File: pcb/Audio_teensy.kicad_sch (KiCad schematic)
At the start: 20 parts, among them J1 0855025008, J2 SSM-114-L-SV-BE, J3 SSM-114-L-SV-BE, J4 MJ-3523-SMT, J5 MJ-3523-SMT, U1 Teensy 3.2, U2 AP7313, U3 SGTL5000

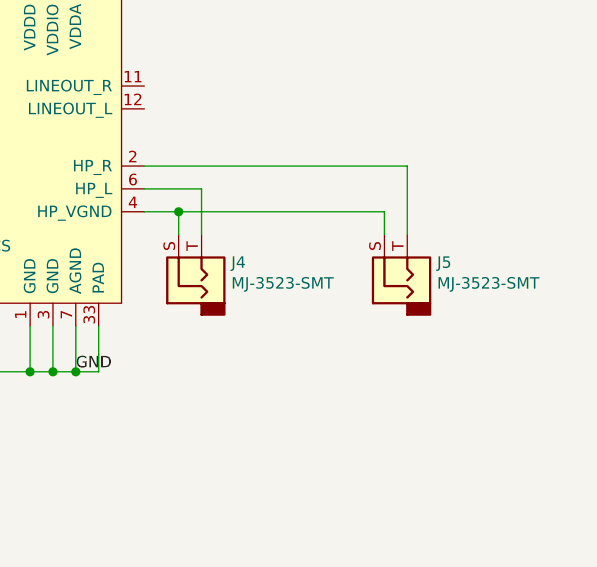
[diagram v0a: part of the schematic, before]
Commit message: changed to through hole components
rearranged mono jacks to point towards opposite sides
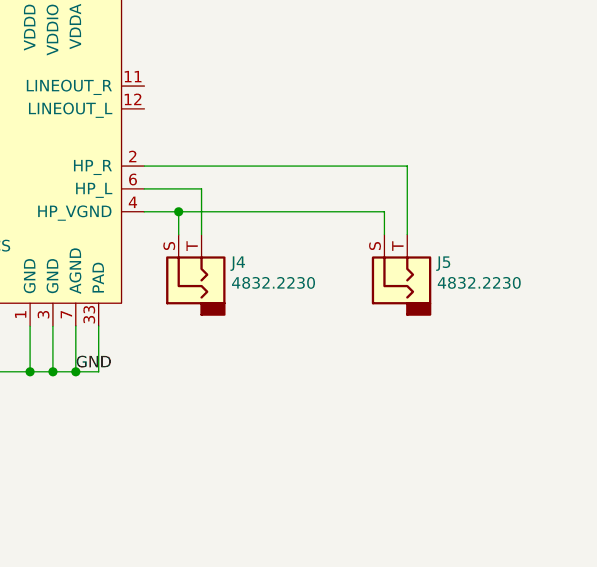
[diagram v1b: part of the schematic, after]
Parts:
- J1: footprint asl_footprints:RJ45_SMD -> asl_footprints:RJ45_THP_Vertical
- J4, J5: value MJ-3523-SMT -> 4832.2230; footprint asl_footprints:MonoJack -> asl_footprints:mono_jack_throughhole
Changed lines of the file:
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@@
   (paper "A4")
   (title_block
-    (date "2019-11-08")
-    (rev "1.1")
+    (date "2021-09-01")
+    (rev "1.2")
   )
   (junction (at 130.81 59.69) (diameter 1.016) (color 0 0 0 0))
@@
       (effects (font (size 1.27 1.27)) (justify right))
     )
-    (property "Value" "MJ-3523-SMT" (id 1) (at 207.772 122.2502 90)
-      (effects (font (size 1.27 1.27)) (justify right))
-    )
-    (property "Footprint" "asl_footprints:MonoJack" (id 2) (at 208.28 121.92 0)
-      (effects (font (size 1.27 1.27)) hide)
-    )
-    (property "Datasheet" "https://www.digikey.com/products/en?keywords=CP-3523MJCT-ND" (id 3) (at 204.47 121.92 0)
+    (property "Value" "4832.2230" (id 1) (at 207.772 122.2502 90)
+      (effects (font (size 1.27 1.27)) (justify right))
+    )
+    (property "Footprint" "asl_footprints:mono_jack_throughhole" (id 2) (at 208.28 121.92 0)
+      (effects (font (size 1.27 1.27)) hide)
+    )
+    (property "Datasheet" "https://www.digikey.com/en/products/detail/4832.2230/486-3417-ND/1731054?itemSeq=375577354" (id 3) (at 204.47 121.92 0)
       (effects (font (size 1.27 1.27)) hide)
     )
@@
       (effects (font (size 1.27 1.27)) (justify right))
     )
-    (property "Value" "MJ-3523-SMT" (id 1) (at 230.632 122.2502 90)
-      (effects (font (size 1.27 1.27)) (justify right))
-    )
-    (property "Footprint" "asl_footprints:MonoJack" (id 2) (at 231.14 121.92 0)
-      (effects (font (size 1.27 1.27)) hide)
-    )
-    (property "Datasheet" "https://www.digikey.com/products/en?keywords=CP-3523MJCT-ND" (id 3) (at 227.33 121.92 0)
+    (property "Value" "4832.2230" (id 1) (at 230.632 122.2502 90)
+      (effects (font (size 1.27 1.27)) (justify right))
+    )
+    (property "Footprint" "asl_footprints:mono_jack_throughhole" (id 2) (at 231.14 121.92 0)
+      (effects (font (size 1.27 1.27)) hide)
+    )
+    (property "Datasheet" "https://www.digikey.com/en/products/detail/4832.2230/486-3417-ND/1731054?itemSeq=375577354" (id 3) (at 227.33 121.92 0)
       (effects (font (size 1.27 1.27)) hide)
     )
@@
       (effects (font (size 1.27 1.27)) (justify left))
     )
-    (property "Footprint" "asl_footprints:RJ45_SMD" (id 2) (at 54.61 74.93 0)
+    (property "Footprint" "asl_footprints:RJ45_THP_Vertical" (id 2) (at 54.61 74.93 0)
       (effects (font (size 1.27 1.27)) hide)
     )
@@
     )
     (path "/00000000-0000-0000-0000-00005dbb4566"
-      (reference "J1") (unit 1) (value "0855025008") (footprint "asl_footprints:RJ45_SMD")
+      (reference "J1") (unit 1) (value "0855025008") (footprint "asl_footprints:RJ45_THP_Vertical")
     )
     (path "/00000000-0000-0000-0000-00005dc200bf"
@@
     )
     (path "/00000000-0000-0000-0000-00005dbb2449"
-      (reference "J4") (unit 1) (value "MJ-3523-SMT") (footprint "asl_footprints:MonoJack")
+      (reference "J4") (unit 1) (value "4832.2230") (footprint "asl_footprints:mono_jack_throughhole")
     )
     (path "/00000000-0000-0000-0000-00005dbb640c"
-      (reference "J5") (unit 1) (value "MJ-3523-SMT") (footprint "asl_footprints:MonoJack")
+      (reference "J5") (unit 1) (value "4832.2230") (footprint "asl_footprints:mono_jack_throughhole")
     )
     (path "/00000000-0000-0000-0000-00005dbd3e4c"

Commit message: pcb v1.3
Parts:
- renumbered C6 to C4, C7 to C5, C5 to C6, C4 to C7, J4 to J2, J5 to J3, J2 to J4, J3 to J5, R3 to R1, R1 to R3, U2 to U1, U1 to U2
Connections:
- no-connect marks 20 -> 22
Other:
- note added: "Left"
- note added: "Right"
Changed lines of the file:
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@@
   (paper "A4")
   (title_block
-    (date "2021-09-01")
-    (rev "1.2")
+    (date "2021-10-12")
+    (rev "1.3")
   )
   (junction (at 130.81 59.69) (diameter 1.016) (color 0 0 0 0))
@@
   (no_connect (at 144.78 105.41))
   (no_connect (at 144.78 107.95))
+  (no_connect (at 198.12 100.33))
+  (no_connect (at 198.12 102.87))
   (wire (pts (xy 64.77 80.01) (xy 93.98 80.01))
     (stroke (width 0) (type solid) (color 0 0 0 0))
@@
     (effects (font (size 1.27 1.27)) (justify left bottom))
   )
+  (text "Left" (at 203.2 129.54 0)
+    (effects (font (size 1.27 1.27)) (justify left bottom))
+  )
+  (text "Right" (at 224.79 129.54 0)
+    (effects (font (size 1.27 1.27)) (justify left bottom))
+  )
   (label "GND" (at 66.04 82.55 0)
     (effects (font (size 1.27 1.27)) (justify left bottom))
@@
   (symbol (lib_id "Device:R_Small_US") (at 86.36 110.49 0) (unit 1)
     (in_bom yes) (on_board yes)
-    (property "Reference" "R1" (id 0) (at 88.0872 109.3216 0)
+    (property "Reference" "R3" (id 0) (at 88.0872 109.3216 0)
       (effects (font (size 1.27 1.27)) (justify left))
     )
@@
   (symbol (lib_id "Device:R_Small_US") (at 158.75 90.17 0) (unit 1)
     (in_bom yes) (on_board yes)
-    (property "Reference" "R3" (id 0) (at 160.4772 89.0016 0)
+    (property "Reference" "R1" (id 0) (at 160.4772 89.0016 0)
       (effects (font (size 1.27 1.27)) (justify left))
     )
@@
   (symbol (lib_id "Device:C") (at 153.67 124.46 0) (unit 1)
     (in_bom yes) (on_board yes)
-    (property "Reference" "C4" (id 0) (at 156.591 123.2916 0)
+    (property "Reference" "C7" (id 0) (at 156.591 123.2916 0)
       (effects (font (size 1.27 1.27)) (justify left))
     )
@@
   (symbol (lib_id "Device:C") (at 173.99 74.93 0) (unit 1)
     (in_bom yes) (on_board yes)
-    (property "Reference" "C5" (id 0) (at 176.911 73.7616 0)
+    (property "Reference" "C6" (id 0) (at 176.911 73.7616 0)
       (effects (font (size 1.27 1.27)) (justify left))
     )
@@
   (symbol (lib_id "Device:C") (at 203.2 63.5 0) (mirror x) (unit 1)
     (in_bom yes) (on_board yes)
-    (property "Reference" "C6" (id 0) (at 200.3044 62.3316 0)
+    (property "Reference" "C4" (id 0) (at 200.3044 62.3316 0)
       (effects (font (size 1.27 1.27)) (justify right))
     )
@@
   (symbol (lib_id "Device:C") (at 215.9 63.5 0) (mirror x) (unit 1)
     (in_bom yes) (on_board yes)
-    (property "Reference" "C7" (id 0) (at 213.0044 62.3316 0)
+    (property "Reference" "C5" (id 0) (at 213.0044 62.3316 0)
       (effects (font (size 1.27 1.27)) (justify right))
     )
@@
   (symbol (lib_id "asl_symbols:MonoJack") (at 204.47 121.92 90) (unit 1)
     (in_bom yes) (on_board yes)
-    (property "Reference" "J4" (id 0) (at 207.772 119.9388 90)
+    (property "Reference" "J2" (id 0) (at 207.772 119.9388 90)
       (effects (font (size 1.27 1.27)) (justify right))
     )
@@
   (symbol (lib_id "asl_symbols:MonoJack") (at 227.33 121.92 90) (unit 1)
     (in_bom yes) (on_board yes)
-    (property "Reference" "J5" (id 0) (at 230.632 119.9388 90)
+    (property "Reference" "J3" (id 0) (at 230.632 119.9388 90)
       (effects (font (size 1.27 1.27)) (justify right))
     )
@@
   (symbol (lib_id "Connector:Conn_01x14_Female") (at 64.77 142.24 0) (unit 1)
     (in_bom yes) (on_board yes)
-    (property "Reference" "J2" (id 0) (at 65.4812 142.8496 0)
+    (property "Reference" "J4" (id 0) (at 65.4812 142.8496 0)
       (effects (font (size 1.27 1.27)) (justify left))
     )
@@
   (symbol (lib_id "Connector:Conn_01x14_Female") (at 91.44 142.24 0) (unit 1)
     (in_bom yes) (on_board yes)
-    (property "Reference" "J3" (id 0) (at 92.1512 142.8496 0)
+    (property "Reference" "J5" (id 0) (at 92.1512 142.8496 0)
       (effects (font (size 1.27 1.27)) (justify left))
     )
@@
   (symbol (lib_id "asl_symbols:AP7313") (at 162.56 69.85 0) (unit 1)
     (in_bom yes) (on_board yes)
-    (property "Reference" "U2" (id 0) (at 162.56 60.96 0))
+    (property "Reference" "U1" (id 0) (at 162.56 60.96 0))
     (property "Value" "AP7313" (id 1) (at 162.56 63.5 0))
     (property "Footprint" "Package_TO_SOT_SMD:TSOT-23" (id 2) (at 162.56 72.39 0)
@@
   (symbol (lib_id "asl_symbols:Teensy3.2_smd") (at 119.38 99.06 0) (unit 1)
     (in_bom yes) (on_board yes)
-    (property "Reference" "U1" (id 0) (at 101.6 73.66 0)
+    (property "Reference" "U2" (id 0) (at 101.6 73.66 0)
       (effects (font (size 1.524 1.524)))
     )
@@
       (reference "C3") (unit 1) (value "100nF") (footprint "Capacitor_SMD:C_0603_1608Metric")
     )
+    (path "/00000000-0000-0000-0000-00005dbf5f5d"
+      (reference "C4") (unit 1) (value "2.2µF") (footprint "Capacitor_SMD:C_0603_1608Metric")
+    )
+    (path "/00000000-0000-0000-0000-00005dbf64c7"
+      (reference "C5") (unit 1) (value "100nF") (footprint "Capacitor_SMD:C_0603_1608Metric")
+    )
+    (path "/00000000-0000-0000-0000-00005dba7323"
+      (reference "C6") (unit 1) (value "1.0µF") (footprint "Capacitor_SMD:C_0603_1608Metric")
+    )
     (path "/00000000-0000-0000-0000-00005dbba3e1"
-      (reference "C4") (unit 1) (value "150nF") (footprint "Capacitor_SMD:C_0603_1608Metric")
-    )
-    (path "/00000000-0000-0000-0000-00005dba7323"
-      (reference "C5") (unit 1) (value "1.0µF") (footprint "Capacitor_SMD:C_0603_1608Metric")
-    )
-    (path "/00000000-0000-0000-0000-00005dbf5f5d"
-      (reference "C6") (unit 1) (value "2.2µF") (footprint "Capacitor_SMD:C_0603_1608Metric")
-    )
-    (path "/00000000-0000-0000-0000-00005dbf64c7"
-      (reference "C7") (unit 1) (value "100nF") (footprint "Capacitor_SMD:C_0603_1608Metric")
+      (reference "C7") (unit 1) (value "150nF") (footprint "Capacitor_SMD:C_0603_1608Metric")
     )
     (path "/00000000-0000-0000-0000-00005dbb8672"
@@
       (reference "J1") (unit 1) (value "0855025008") (footprint "asl_footprints:RJ45_THP_Vertical")
     )
+    (path "/00000000-0000-0000-0000-00005dbb2449"
+      (reference "J2") (unit 1) (value "4832.2230") (footprint "asl_footprints:mono_jack_throughhole")
+    )
+    (path "/00000000-0000-0000-0000-00005dbb640c"
+      (reference "J3") (unit 1) (value "4832.2230") (footprint "asl_footprints:mono_jack_throughhole")
+    )
     (path "/00000000-0000-0000-0000-00005dc200bf"
-      (reference "J2") (unit 1) (value "SSM-114-L-SV-BE") (footprint "Connector_PinHeader_2.54mm:PinHeader_1x14_P2.54mm_Vertical_SMD_Pin1Left")
+      (reference "J4") (unit 1) (value "SSM-114-L-SV-BE") (footprint "Connector_PinHeader_2.54mm:PinHeader_1x14_P2.54mm_Vertical_SMD_Pin1Left")
     )
     (path "/00000000-0000-0000-0000-00005dc27049"
-      (reference "J3") (unit 1) (value "SSM-114-L-SV-BE") (footprint "Connector_PinHeader_2.54mm:PinHeader_1x14_P2.54mm_Vertical_SMD_Pin1Left")
-    )
-    (path "/00000000-0000-0000-0000-00005dbb2449"
-      (reference "J4") (unit 1) (value "4832.2230") (footprint "asl_footprints:mono_jack_throughhole")
-    )
-    (path "/00000000-0000-0000-0000-00005dbb640c"
-      (reference "J5") (unit 1) (value "4832.2230") (footprint "asl_footprints:mono_jack_throughhole")
-    )
-    (path "/00000000-0000-0000-0000-00005dbd3e4c"
-      (reference "R1") (unit 1) (value "100Ω") (footprint "Resistor_SMD:R_0603_1608Metric")
+      (reference "J5") (unit 1) (value "SSM-114-L-SV-BE") (footprint "Connector_PinHeader_2.54mm:PinHeader_1x14_P2.54mm_Vertical_SMD_Pin1Left")
+    )
+    (path "/00000000-0000-0000-0000-00005dbbc182"
+      (reference "R1") (unit 1) (value "2.2KΩ") (footprint "Resistor_SMD:R_0603_1608Metric")
     )
     (path "/00000000-0000-0000-0000-00005dbbdf2a"
       (reference "R2") (unit 1) (value "2.2KΩ") (footprint "Resistor_SMD:R_0603_1608Metric")
     )
-    (path "/00000000-0000-0000-0000-00005dbbc182"
-      (reference "R3") (unit 1) (value "2.2KΩ") (footprint "Resistor_SMD:R_0603_1608Metric")
+    (path "/00000000-0000-0000-0000-00005dbd3e4c"
+      (reference "R3") (unit 1) (value "100Ω") (footprint "Resistor_SMD:R_0603_1608Metric")
+    )
+    (path "/00000000-0000-0000-0000-00005dba0e92"
+      (reference "U1") (unit 1) (value "AP7313") (footprint "Package_TO_SOT_SMD:TSOT-23")
     )
     (path "/00000000-0000-0000-0000-00005dc565c7"
-      (reference "U1") (unit 1) (value "Teensy 3.2") (footprint "asl_footprints:Teensy30_31_32_LC_SMD")
-    )
-    (path "/00000000-0000-0000-0000-00005dba0e92"
-      (reference "U2") (unit 1) (value "AP7313") (footprint "Package_TO_SOT_SMD:TSOT-23")
+      (reference "U2") (unit 1) (value "Teensy 3.2") (footprint "asl_footprints:Teensy30_31_32_LC_SMD")
     )
     (path "/00000000-0000-0000-0000-00005dbb136f"
